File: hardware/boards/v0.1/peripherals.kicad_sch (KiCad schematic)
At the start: 6 parts, among them IC2 DA7280-00FVC, J6 VLV101040A, U21 LSM6DS3

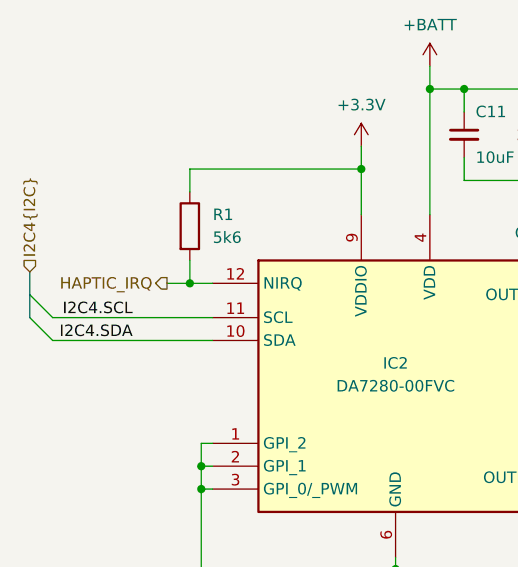
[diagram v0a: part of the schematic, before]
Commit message: chore: make ERC happy
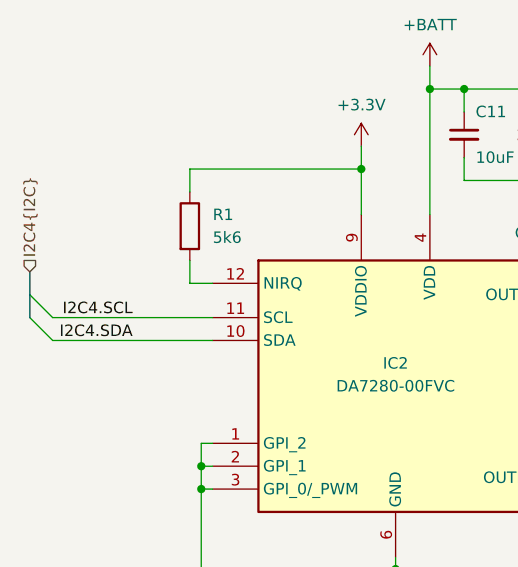
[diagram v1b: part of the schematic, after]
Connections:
- net HAPTIC_IRQ: no longer names the net of IC2.12 (NIRQ), R1.2
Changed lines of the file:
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@@
-	)
-	(junction
-		(at 39.37 49.53)
-		(diameter 0)
-		(color 0 0 0 0)
 	)
 	(junction
@@
 		(pts
 			(xy 40.64 81.28) (xy 62.23 81.28)
-		)
-		(stroke
-			(width 0)
-			(type default)
-		)
-	)
-	(wire
-		(pts
-			(xy 36.83 49.53) (xy 39.37 49.53)
 		)
 		(stroke
@@
 		)
 	)
-	(hierarchical_label "HAPTIC_IRQ"
-		(shape output)
-		(at 36.83 49.53 180)
-		(effects
-			(font
-				(size 1.27 1.27)
-				(thickness 0.1588)
-			)
-			(justify right)
-		)
-	)

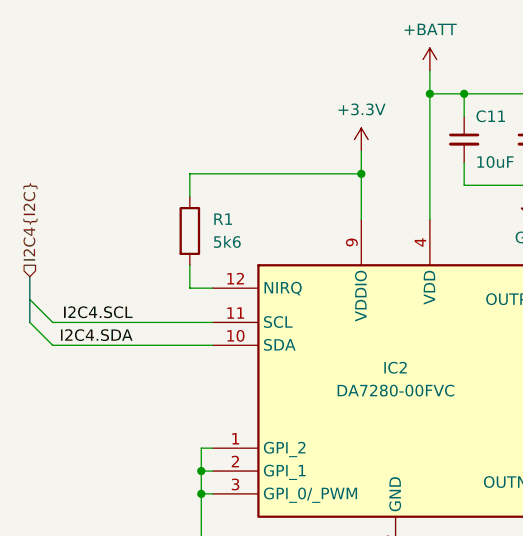
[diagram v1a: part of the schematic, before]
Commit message: feat: clean up routing, remove metronome light
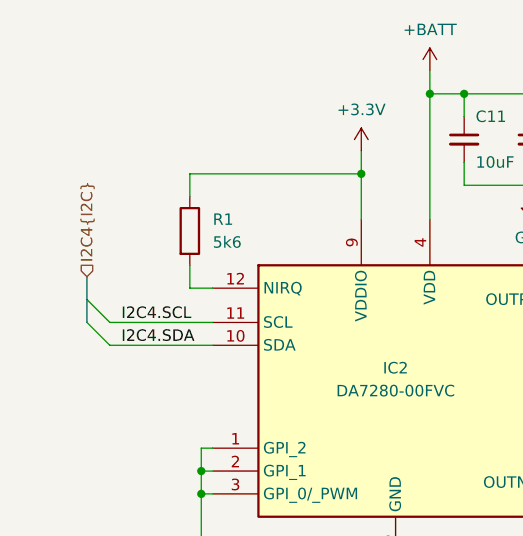
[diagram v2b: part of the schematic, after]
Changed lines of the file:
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@@
 	)
 	(bus_entry
-		(at 24.13 55.88)
+		(at 30.48 55.88)
 		(size -2.54 -2.54)
 		(stroke
@@
 	)
 	(bus_entry
-		(at 24.13 53.34)
+		(at 30.48 53.34)
 		(size -2.54 -2.54)
 		(stroke
@@
 	(wire
 		(pts
-			(xy 24.13 53.34) (xy 41.91 53.34)
+			(xy 30.48 53.34) (xy 41.91 53.34)
 		)
 		(stroke
@@
 	(wire
 		(pts
-			(xy 24.13 55.88) (xy 41.91 55.88)
+			(xy 30.48 55.88) (xy 41.91 55.88)
 		)
 		(stroke
@@
 	(bus
 		(pts
-			(xy 21.59 48.26) (xy 21.59 50.8)
+			(xy 27.94 48.26) (xy 27.94 50.8)
 		)
 		(stroke
@@
 	(bus
 		(pts
-			(xy 21.59 50.8) (xy 21.59 53.34)
+			(xy 27.94 50.8) (xy 27.94 53.34)
 		)
 		(stroke
@@
 	)
 	(label "I2C4.SCL"
-		(at 33.02 53.34 180)
+		(at 31.75 53.34 0)
 		(effects
 			(font
 				(size 1.27 1.27)
 			)
-			(justify right bottom)
+			(justify left bottom)
 		)
 	)
@@
 	)
 	(label "I2C4.SDA"
-		(at 33.02 55.88 180)
+		(at 31.75 55.88 0)
 		(effects
 			(font
 				(size 1.27 1.27)
 			)
-			(justify right bottom)
+			(justify left bottom)
 		)
 	)
@@
 	(hierarchical_label "I2C4{I2C}"
 		(shape input)
-		(at 21.59 48.26 90)
+		(at 27.94 48.26 90)
 		(effects
 			(font
@@
 			)
 		)
-		(property "Datasheet" "https://www.dialog-semiconductor.com/sites/default/files/da7280_datasheet_3v0.pdf"
+		(property "Datasheet" "https://www.renesas.com/en/document/dst/da7280-datasheet?language=en&utm_nooverride=1"
 			(at 99.06 246.99 0)
 			(effects

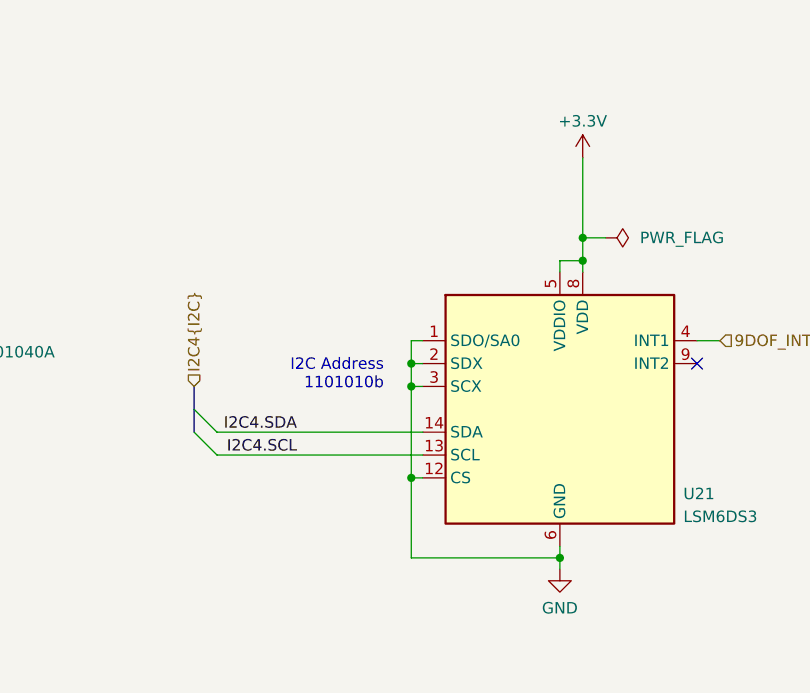
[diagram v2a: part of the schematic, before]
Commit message: feat: routing cleanup and start of BOM selection
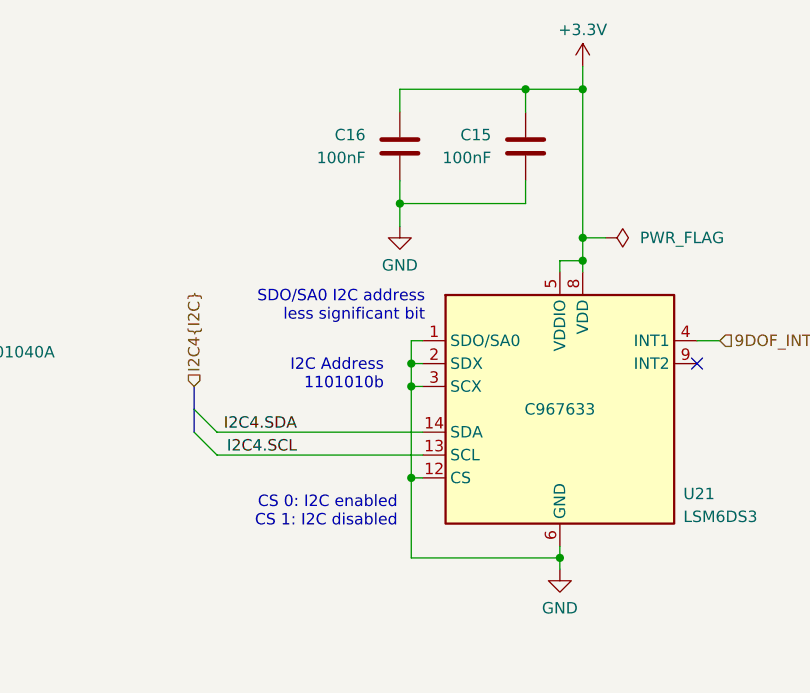
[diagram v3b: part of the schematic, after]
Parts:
- added C15, C16: 100nF, Capacitor_SMD:C_0603_1608Metric, symbol Device:C
- IC2: JLC (none) -> C2155359
- U21: JLC (none) -> C967633
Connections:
- net +3.3V: now also C15.1, C16.1
- net GND: now also C15.2, C16.2
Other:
- note added: "CS 0: I2C enabled CS 1: I2C disabled"
- note added: "SDO/SA0 I2C address less significant bit"

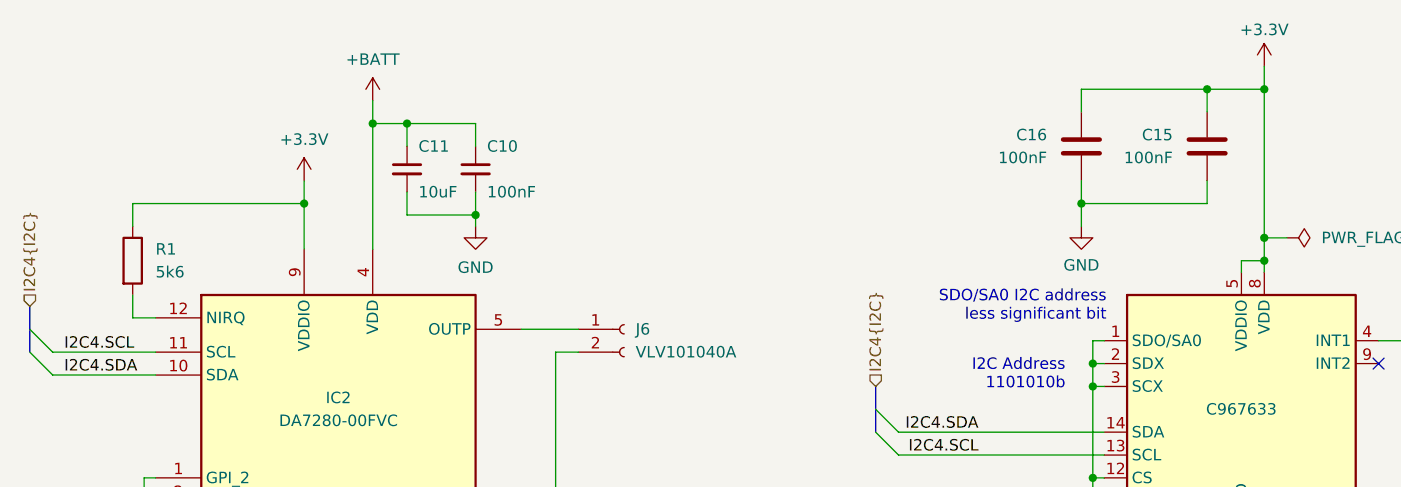
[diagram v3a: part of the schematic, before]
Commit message: feat: update various components to 0402
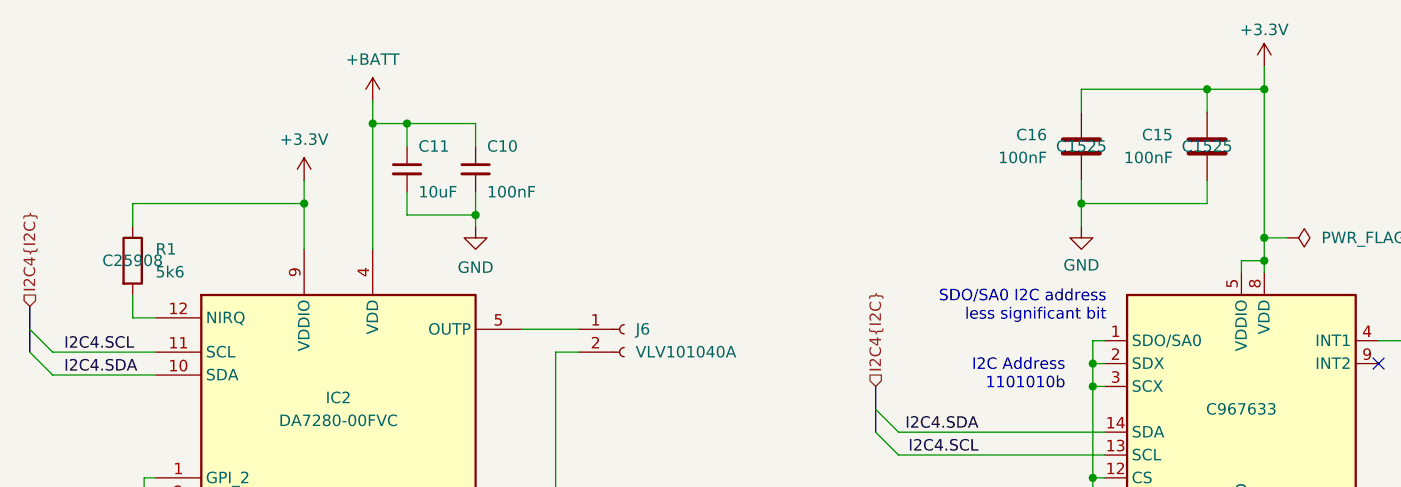
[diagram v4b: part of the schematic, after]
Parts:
- C10: footprint Capacitor_SMD:C_0603_1608Metric -> Capacitor_SMD:C_0402_1005Metric; JLC (none) -> C1525
- C11: footprint (none) -> Capacitor_SMD:C_0402_1005Metric
- C15, C16: JLC (none) -> C1525
- IC2: Mouser Part Number 724-DA7280-00FVC -> (none); Mouser Price/Stock https://www.mouser.co.uk/ProductDetail/Renesas-Dialog/DA728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 -> (none)
- R1: footprint Resistor_SMD:R_0603_1608Metric -> Resistor_SMD:R_0402_1005Metric; JLC (none) -> C25908
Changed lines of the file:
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@@
 			)
 		)
-		(property "Footprint" "Resistor_SMD:R_0603_1608Metric"
+		(property "Footprint" "Resistor_SMD:R_0402_1005Metric"
 			(at 37.592 43.18 90)
 			(effects
@@
 		)
 		(property "Connector" ""
+			(at 39.37 43.18 0)
+			(effects
+				(font
+					(size 1.27 1.27)
+				)
+			)
+		)
+		(property "JLC" "C25908"
 			(at 39.37 43.18 0)
 			(effects
@@
 			)
 		)
+		(property "JLC" "C1525"
+			(at 144.78 30.48 0)
+			(effects
+				(font
+					(size 1.27 1.27)
+				)
+			)
+		)
 		(pin "1"
 		)
@@
 			)
 		)
-		(property "Mouser Part Number" "724-DA7280-00FVC"
-			(at 99.06 546.99 0)
-			(effects
-				(font
-					(size 1.27 1.27)
-				)
-				(justify left top)
-				(hide yes)
-			)
-		)
-		(property "Mouser Price/Stock" "https://www.mouser.co.uk/ProductDetail/Renesas-Dialog/DA7280-00FVC?qs=byeeYqUIh0PDtQ9ScBbgLA%3D%3D"
-			(at 99.06 646.99 0)
-			(effects
-				(font
-					(size 1.27 1.27)
-				)
-				(justify left top)
-				(hide yes)
-			)
-		)
 		(property "Manufacturer_Name" "Renesas Electronics"
 			(at 99.06 746.99 0)
@@
 			)
 		)
-		(property "Arrow Part Number" ""
-			(at 162.56 59.69 0)
-			(effects
-				(font
-					(size 1.27 1.27)
-				)
-			)
-		)
-		(property "Arrow Price/Stock" ""
-			(at 162.56 59.69 0)
-			(effects
-				(font
-					(size 1.27 1.27)
-				)
-			)
-		)
 		(property "MANUFACTURER" ""
 			(at 162.56 59.69 0)
@@
 		)
 		(property "MAXIMUM_PACKAGE_HEIGHT" ""
-			(at 162.56 59.69 0)
-			(effects
-				(font
-					(size 1.27 1.27)
-				)
-			)
-		)
-		(property "PARTREV" ""
-			(at 162.56 59.69 0)
-			(effects
-				(font
-					(size 1.27 1.27)
-				)
-			)
-		)
-		(property "STANDARD" ""
 			(at 162.56 59.69 0)
 			(effects
@@
 			)
 		)
-		(property "Footprint" "Capacitor_SMD:C_0603_1608Metric"
+		(property "Footprint" "Capacitor_SMD:C_0402_1005Metric"
 			(at 77.47 33.02 0)
 			(effects
@@
 					(size 1.27 1.27)
 				)
+			)
+		)
+		(property "JLC" "C1525"
+			(at 77.47 33.02 0)
+			(effects
+				(font
+					(size 1.27 1.27)
+				)
+				(hide yes)
 			)
 		)
@@
 			)
 		)
+		(property "JLC" "C1525"
+			(at 158.75 30.48 0)
+			(effects
+				(font
+					(size 1.27 1.27)
+				)
+			)
+		)
 		(pin "1"
 		)
@@
 			)
 		)
-		(property "Footprint" ""
+		(property "Footprint" "Capacitor_SMD:C_0402_1005Metric"
 			(at 69.85 33.02 0)
 			(effects
@@
 			)
 		)
+		(property "JLC" ""
+			(at 69.85 33.02 0)
+			(effects
+				(font
+					(size 1.27 1.27)
+				)
+				(hide yes)
+			)
+		)

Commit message: feat: various routing cleanup, add SD flash
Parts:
- C11: JLC (none) -> C15525
- C15, C16: footprint Capacitor_SMD:C_0603_1608Metric -> Capacitor_SMD:C_0402_1005Metric
- J6: now left out of the parts list
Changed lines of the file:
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@@
+			)
+		)
+		(property "Part" ""
+			(at 39.37 43.18 0)
+			(effects
+				(font
+					(size 1.27 1.27)
+				)
 			)
 		)
@@
 			)
 		)
-		(property "Footprint" "Capacitor_SMD:C_0603_1608Metric"
+		(property "Footprint" "Capacitor_SMD:C_0402_1005Metric"
 			(at 143.8148 34.29 0)
 			(effects
@@
 			)
 		)
+		(property "Part" ""
+			(at 144.78 30.48 0)
+			(effects
+				(font
+					(size 1.27 1.27)
+				)
+			)
+		)
 		(pin "1"
 		)
@@
 			)
 		)
+		(property "Part" ""
+			(at 62.23 59.69 0)
+			(effects
+				(font
+					(size 1.27 1.27)
+				)
+			)
+		)
 		(pin "1"
 		)
@@
 		)
 		(property "Connector" ""
+			(at 162.56 59.69 0)
+			(effects
+				(font
+					(size 1.27 1.27)
+				)
+			)
+		)
+		(property "Part" ""
 			(at 162.56 59.69 0)
 			(effects
@@
 			)
 		)
+		(property "Part" ""
+			(at 77.47 33.02 0)
+			(effects
+				(font
+					(size 1.27 1.27)
+				)
+			)
+		)
 		(pin "1"
 		)
@@
 			)
 		)
-		(property "Footprint" "Capacitor_SMD:C_0603_1608Metric"
+		(property "Footprint" "Capacitor_SMD:C_0402_1005Metric"
 			(at 157.7848 34.29 0)
 			(effects
@@
 		)
 		(property "JLC" "C1525"
+			(at 158.75 30.48 0)
+			(effects
+				(font
+					(size 1.27 1.27)
+				)
+			)
+		)
+		(property "Part" ""
 			(at 158.75 30.48 0)
 			(effects
@@
 			)
 		)
-		(property "JLC" ""
+		(property "JLC" "C15525"
 			(at 69.85 33.02 0)
 			(effects
@@
 				)
 				(hide yes)
+			)
+		)
+		(property "Part" ""
+			(at 69.85 33.02 0)
+			(effects
+				(font
+					(size 1.27 1.27)
+				)
 			)
 		)
@@
 		(unit 1)
 		(exclude_from_sim no)
-		(in_bom yes)
+		(in_bom no)
 		(on_board yes)
 		(dnp no)
@@
 			)
 		)
+		(property "Part" ""
+			(at 93.98 50.8 0)
+			(effects
+				(font
+					(size 1.27 1.27)
+				)
+			)
+		)
